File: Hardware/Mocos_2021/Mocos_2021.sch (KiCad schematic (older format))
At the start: 104 parts, among them IC1 TC2117, J1 USB_B_Mini, J2 SERIAL PORT, J3 Programming, Q1 IRFS7530, Q2 IRFS7530, Q3 IRFS7530, Q4 IRFS7530, Q5 IRFS7530, Q6 IRFS7530, U1 DRV8302, U2 STM32F40X_LQFP64, X1 8MHz, 10ppm

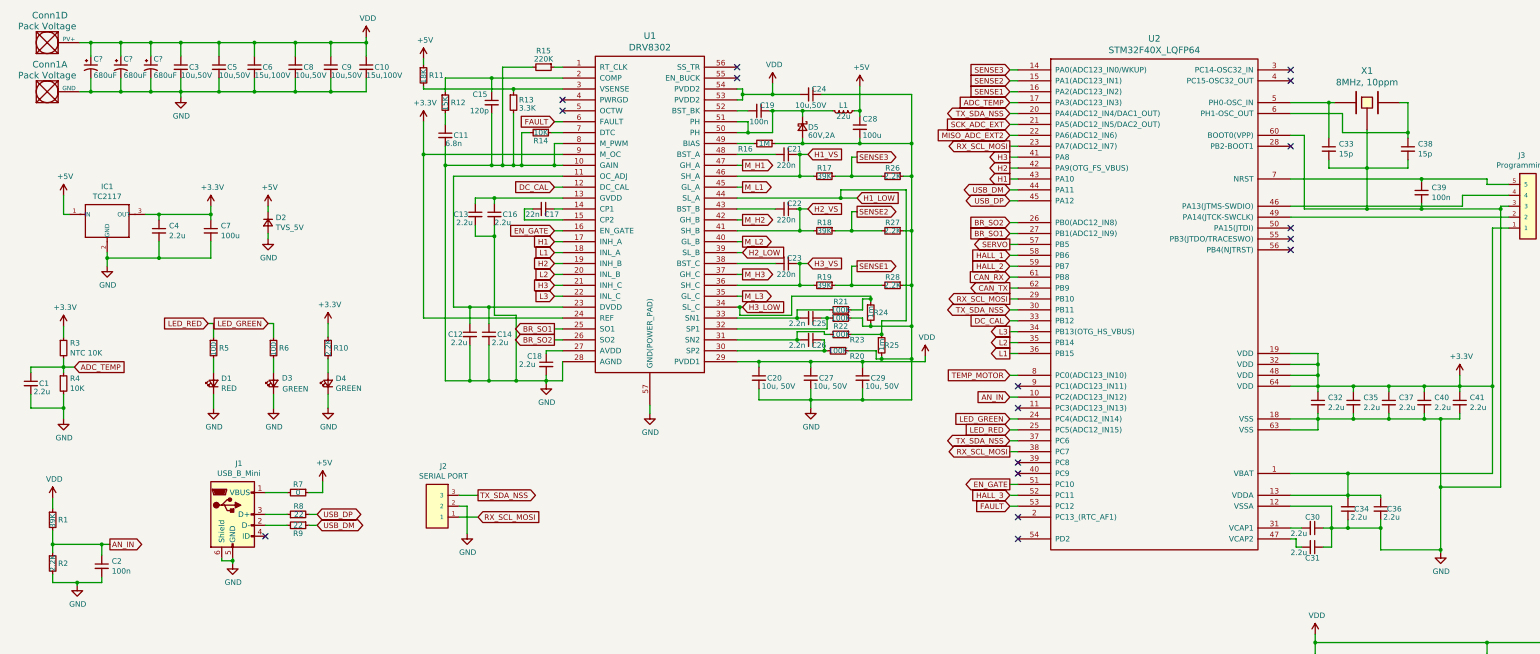
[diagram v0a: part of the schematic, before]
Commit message: Added footprints to board
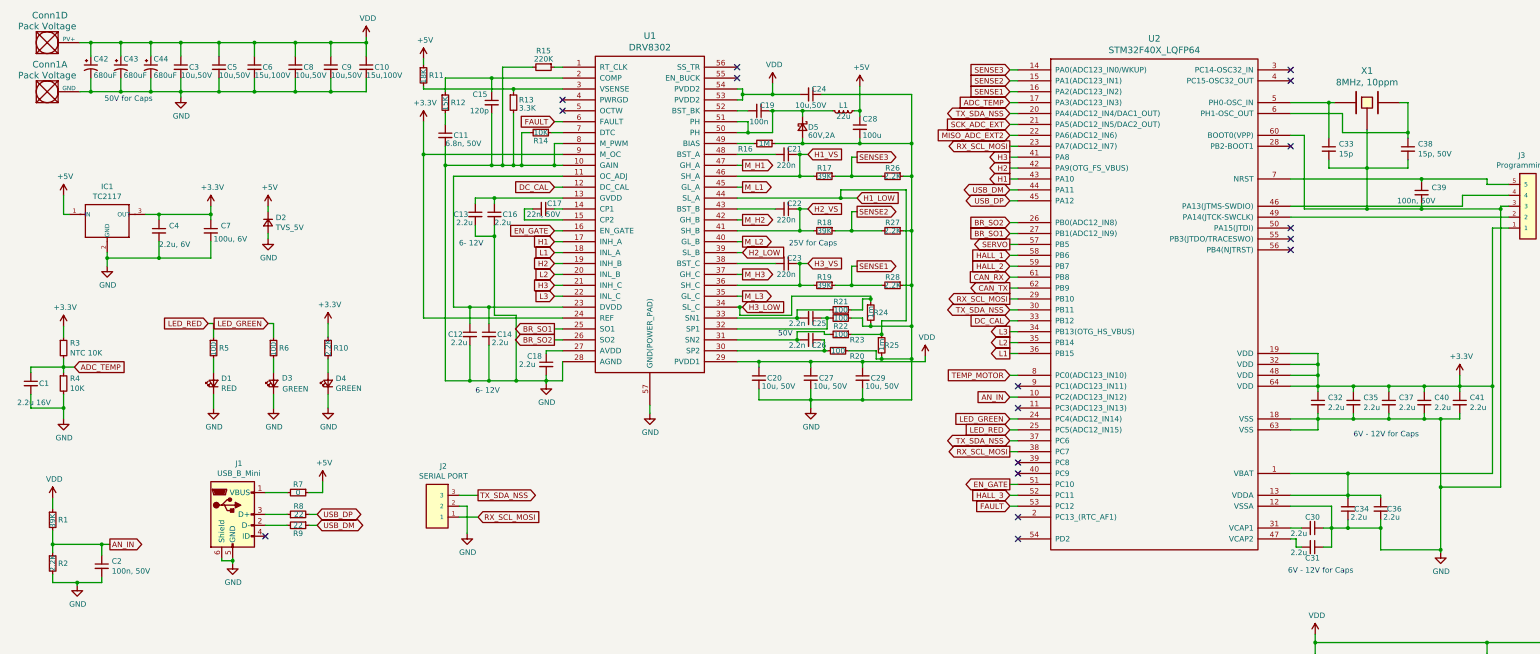
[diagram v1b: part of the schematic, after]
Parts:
- C1: value 2.2u -> 2.2u 16V; footprint Capacitor_SMD:C_1206_3216Metric_Pad1.33x1.80mm_HandSolder -> Capacitor_SMD:C_0402_1005Metric_Pad0.74x0.62mm_HandSolder
- C10, C28, C6: footprint (none) -> Capacitor_SMD:C_2220_5650Metric_Pad1.97x5.40mm_HandSolder
- C11: value 6.8n -> 6.8n, 50V; footprint (none) -> Capacitor_SMD:C_0603_1608Metric_Pad1.08x0.95mm_HandSolder
- C12, C13, C14, C15, C16, C18, C25, C26, C30, C31, C32, C34, C35, C36, C37, C40, C41: footprint (none) -> Capacitor_SMD:C_0402_1005Metric_Pad0.74x0.62mm_HandSolder
- C17: value 22n -> 22n, 50V; footprint (none) -> Capacitor_SMD:C_0402_1005Metric_Pad0.74x0.62mm_HandSolder
- C19, C33: footprint (none) -> Capacitor_SMD:C_0603_1608Metric_Pad1.08x0.95mm_HandSolder
- C2: value 100n -> 100n, 50V
- C20, C24, C27, C29, C5, C8, C9: footprint (none) -> Capacitor_SMD:C_1210_3225Metric_Pad1.33x2.70mm_HandSolder
- C21, C22, C23: footprint (none) -> Capacitor_SMD:C_0805_2012Metric_Pad1.18x1.45mm_HandSolder
- C3: footprint Capacitor_SMD:C_0603_1608Metric_Pad1.08x0.95mm_HandSolder -> Capacitor_SMD:C_1210_3225Metric_Pad1.33x2.70mm_HandSolder
- C38: value 15p -> 15p, 50V; footprint (none) -> Capacitor_SMD:C_0603_1608Metric_Pad1.08x0.95mm_HandSolder
- C39: value 100n -> 100n, 50V; footprint (none) -> Capacitor_SMD:C_0603_1608Metric_Pad1.08x0.95mm_HandSolder
- C4: value 2.2u -> 2.2u, 6V; footprint (none) -> Capacitor_SMD:C_0402_1005Metric_Pad0.74x0.62mm_HandSolder
- C42, C43, C44: renamed from C?; footprint (none) -> Capacitor_THT:CP_Radial_D16.0mm_P7.50mm
- C7: value 100u -> 100u, 6V; footprint (none) -> Capacitor_SMD:C_0402_1005Metric_Pad0.74x0.62mm_HandSolder
- Conn1: footprint (none) -> MRDT_Connectors:Anderson_2_Vertical_Sidy_by_Side
- Conn2, Conn3, Conn4: footprint (none) -> MRDT_Connectors:Anderson_2_Horizontal_Side_by_Side
- D1, D3, D4: footprint (none) -> LED_SMD:LED_0603_1608Metric_Pad1.05x0.95mm_HandSolder
- D2: footprint (none) -> Diode_SMD:D_SMA_Handsoldering
- D5: footprint (none) -> Diode_SMD:D_SOD-123F
- J1: footprint (none) -> crf1:mini_USB_gnd
- L1: footprint (none) -> crf1:inductor_74435580680
- Q1, Q2, Q3, Q4, Q5, Q6: footprint (none) -> Package_TO_SOT_SMD:TO-263-7_TabPin4
- R1, R10, R11, R12, R13, R14, R15, R16, R17, R18, R19, R2, R26, R27, R28, R29, R3, R30, R31, R32, R33, R34, R35, R36, R37, R4, R5, R6, R7, R8, R9: footprint (none) -> Resistor_SMD:R_0603_1608Metric_Pad0.98x0.95mm_HandSolder
- R20, R21, R22, R23: value 100K -> 100; footprint (none) -> Resistor_SMD:R_0603_1608Metric_Pad0.98x0.95mm_HandSolder
- R24, R25: footprint (none) -> crf1:WSLP2726
- U1: footprint (none) -> crf1:TSSOP-56-PP
- U2: footprint (none) -> crf1:lqfp64_pad_mod
- X1: footprint (none) -> crf1:Crystal_5x3mm
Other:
- note added: "25V for Caps"
- note added: "50V"
- note added: "50V for Caps"
- note added: "6- 12V"
- note added: "6V - 12V for Caps"

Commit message: Finished STM32 Layout
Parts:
- removed unit 1 of Conn2
- removed unit 1 of Conn3
- removed unit 1 of Conn4
- removed R7: 0, Resistor_SMD:R_0603_1608Metric_Pad0.98x0.95mm_HandSolder, symbol Device:R_Small
- removed X1: 8MHz, 10ppm, crf1:Crystal_5x3mm, symbol crf_1:CRYSTAL_GROUND_PIN
- added X1: 8MHz, 10ppm, crf1:Crystal_5x3mm, symbol crf_1:CRYSTAL_SMD
- Conn1: footprint MRDT_Connectors:Anderson_2_Vertical_Sidy_by_Side -> MRDT_Connectors:Anderson_2_Horizontal_Side_by_Side_PV
- Conn2: value Phase1 -> Phases; footprint MRDT_Connectors:Anderson_2_Horizontal_Side_by_Side -> MRDT_Connectors:Anderson_3_Horizontal_Side_by_Side
- Conn2: renamed from Conn3; value Phase2 -> Phases; footprint MRDT_Connectors:Anderson_2_Horizontal_Side_by_Side -> MRDT_Connectors:Anderson_3_Horizontal_Side_by_Side
- Conn2: renamed from Conn4; value Phase3 -> Phases; footprint MRDT_Connectors:Anderson_2_Horizontal_Side_by_Side -> MRDT_Connectors:Anderson_3_Horizontal_Side_by_Side
- IC1: footprint crf1:v-reg-78XXS -> crf1:SOT-223
- J1: footprint crf1:mini_USB_gnd -> crf1:USB-UX60R-MB-5ST
- J2: footprint MRDT_Connectors:MOLEX_uF_S_03_Vertical -> MRDT_Connectors:MOLEX_uF_S_03_Horizontal
- J3: footprint MRDT_Connectors:MOLEX_uF_S_05_Vertical -> MRDT_Connectors:MOLEX_uF_S_05_Horizontal
- Q1, Q2, Q3, Q4, Q5, Q6: value IRFS7530 -> IRFZ44ESTRLPBF; footprint Package_TO_SOT_SMD:TO-263-7_TabPin4 -> Package_TO_SOT_SMD:TO-263-3_TabPin4
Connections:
- net GND: now also X1.2 (GND/NC), X1.4 (GND/NC)
- net H1_VS: now also Conn2.1 (GND); no longer Conn2.4 (PV+)
- net H2_VS: now also Conn2.2 (V+Log); no longer Conn2.4 (PV+)
- net H3_VS: now also Conn2.3 (V+Act); no longer Conn2.4 (PV+)
- net at C33.1, U2.5 (PH0-OSC_IN): now also X1.1 (CLK)
- net at C38.1, U2.6 (PH1-OSC_OUT): now also X1.3 (CLK)
- net USB_DM renamed USB-
- net USB_DP renamed USB+
- no-connect marks 17 -> 18

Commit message: Added 3.3V Oki for cleaner layout
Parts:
- removed C11: 6.8n, 50V, Capacitor_SMD:C_0603_1608Metric_Pad1.08x0.95mm_HandSolder, symbol Device:C_Small
- removed C15: 120p, Capacitor_SMD:C_0402_1005Metric_Pad0.74x0.62mm_HandSolder, symbol Device:C_Small
- removed C19: 100n, Capacitor_SMD:C_0603_1608Metric_Pad1.08x0.95mm_HandSolder, symbol Device:C_Small
- removed C24: 10u,50V, Capacitor_SMD:C_1210_3225Metric_Pad1.33x2.70mm_HandSolder, symbol Device:C_Small
- removed C28: 100u, Capacitor_SMD:C_2220_5650Metric_Pad1.97x5.40mm_HandSolder, symbol Device:C_Small
- removed D2: TVS_5V, Diode_SMD:D_SMA_Handsoldering, symbol Device:D_Small
- removed D5: 60V,2A, Diode_SMD:D_SOD-123F, symbol Device:D_Schottky_Small
- removed IC1: TC2117, crf1:SOT-223, symbol crf_1:V-reg
- removed L1: 22u, crf1:inductor_74435580680, symbol Device:L_Small
- removed R11: 18K, Resistor_SMD:R_0603_1608Metric_Pad0.98x0.95mm_HandSolder, symbol Device:R_Small
- removed R12: 15K, Resistor_SMD:R_0603_1608Metric_Pad0.98x0.95mm_HandSolder, symbol Device:R_Small
- removed R13: 3.3K, Resistor_SMD:R_0603_1608Metric_Pad0.98x0.95mm_HandSolder, symbol Device:R_Small
- removed R24, R25: 1m, crf1:WSLP2726, symbol Device:R_Small
- added R11, R7: 1m, crf1:WSLP2726, symbol crf_1:SHUNT
- added U3: 3.3V OKI, MRDT_Devices:OKI_Horizontal, symbol MRDT_Devices:OKI
- Q1, Q2, Q3, Q4, Q5, Q6: footprint Package_TO_SOT_SMD:TO-263-3_TabPin4 -> MRDT_Actives:IRFZ44ESTRLPBF
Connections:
- net +3V3: now also U3.3 (Vo)
- net GND: now also R11.2, R7.2, U3.2 (GND); no longer R20.1, R22.1
- net H1_LOW: now also R7.1; no longer R23.1
- net H3_LOW: now also R11.1; no longer R21.1
- net VDD: now also U3.1 (Vi); no longer U1.53 (PVDD2), U1.54 (PVDD2)
- net at U1.50 (PH): no longer U1.51 (PH)
- net CAN_RX: no longer names the net of U2.61 (PB8)
- net CAN_TX: no longer names the net of U2.62 (PB9)
- net HALL_1: no longer names the net of U2.58 (PB6)
- net HALL_2: no longer names the net of U2.59 (PB7)
- net HALL_3: no longer names the net of U2.52 (PC11)
- net SERVO: no longer names the net of U2.57 (PB5)
- net TEMP_MOTOR: no longer names the net of U2.8 (PC0(ADC123_IN10))
- new net: R20.1, R7.4
- new net: R23.1, R7.3
- new net: R11.4, R22.1
- new net: R11.3, R21.1
- no-connect marks 18 -> 32
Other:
- note added: "Connectors"
- note added: "Indicators"
- note added: "MCU"
- note added: "Mosfet Driver"
- note added: "Mosfets"
- note added: "Power"
- note added: "Temperature Sense and Analog In"
- moved on the sheet: C1, C10, C12, C13, C14, C16, C17, C18, C2, C20, C21, C22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

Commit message: Finished layout and generated Gerbs
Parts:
- U1: value DRV8302 -> DRV8302DCA
- U2: value STM32F40X_LQFP64 -> STM32F405RGT6
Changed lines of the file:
@@
 P 12825 3625
 F 0 "U2" H 12825 6062 60  0000 C CNN
-F 1 "STM32F40X_LQFP64" H 12825 5956 60  0000 C CNN
+F 1 "STM32F405RGT6" H 12825 5956 60  0000 C CNN
 F 2 "crf1:lqfp64_pad_mod" H 12825 3625 60  0001 C CNN
 F 3 "" H 12825 3625 60  0000 C CNN
@@
 AR Path="/613C4F07" Ref="U1"  Part="1"
 F 0 "U1" H 6800 4262 60  0000 C CNN
-F 1 "DRV8302" H 6800 4156 60  0000 C CNN
+F 1 "DRV8302DCA" H 6800 4156 60  0000 C CNN
 F 2 "crf1:TSSOP-56-PP" H 6800 2625 60  0001 C CNN
 F 3 "" H 6800 2625 60  0000 C CNN

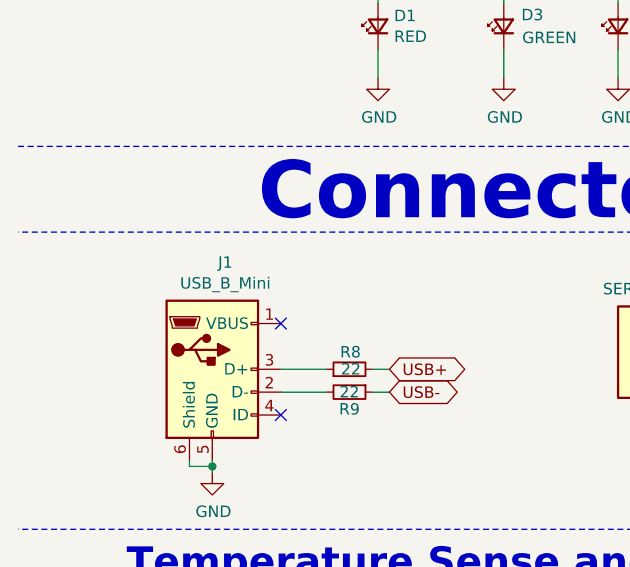
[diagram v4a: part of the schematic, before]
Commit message: Finished BOM and Fixed some Layout errors such as trace tolerance
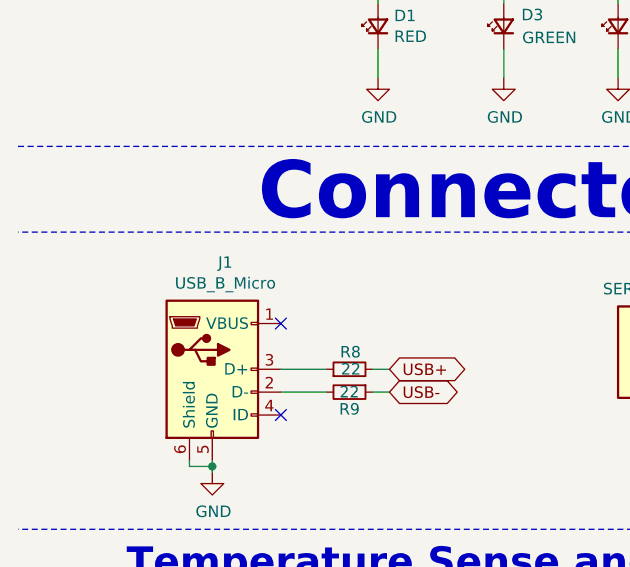
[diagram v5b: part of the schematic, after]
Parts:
- removed J1: USB_B_Mini, crf1:USB-UX60R-MB-5ST, symbol Connector:USB_B_Mini
- added J1: USB_B_Micro, MRDT_Connectors:MOLEX_47346-0001, symbol Connector:USB_B_Micro
- C7: footprint Capacitor_SMD:C_0402_1005Metric_Pad0.74x0.62mm_HandSolder -> Capacitor_SMD:C_0805_2012Metric_Pad1.18x1.45mm_HandSolder
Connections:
- net GND: now also J1.5 (GND), J1.6 (Shield)
- net at R9.2: now also J1.2 (D-)
- net at R8.1: now also J1.3 (D+)
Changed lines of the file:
@@
 F 0 "C7" H 3367 2671 50  0000 L CNN
 F 1 "100u, 6V" H 3300 2550 50  0000 L CNN
-F 2 "Capacitor_SMD:C_0402_1005Metric_Pad0.74x0.62mm_HandSolder" H 3275 2625 50  0001 C CNN
+F 2 "Capacitor_SMD:C_0805_2012Metric_Pad1.18x1.45mm_HandSolder" H 3275 2625 50  0001 C CNN
 F 3 "~" H 3275 2625 50  0001 C CNN
 	1    3275 2625
@@
 	3500 7650 3575 7650
 Connection ~ 3500 7650
-$Comp
-L Connector:USB_B_Mini J1
-U 1 1 6231FC2B
-P 1325 5975
-F 0 "J1" H 1382 6442 50  0000 C CNN
-F 1 "USB_B_Mini" H 1382 6351 50  0000 C CNN
-F 2 "crf1:USB-UX60R-MB-5ST" H 1475 5925 50  0001 C CNN
-F 3 "~" H 1475 5925 50  0001 C CNN
-	1    1325 5975
-	1    0    0    -1
-$EndComp
 $Comp
 L power:GND #PWR010
@@
 	9200 4475 9200 4325
 Connection ~ 9200 4325
+$Comp
+L Connector:USB_B_Micro J1
+U 1 1 612C88A1
+P 1325 5975
+F 0 "J1" H 1382 6442 50  0000 C CNN
+F 1 "USB_B_Micro" H 1382 6351 50  0000 C CNN
+F 2 "MRDT_Connectors:MOLEX_47346-0001" H 1475 5925 50  0001 C CNN
+F 3 "~" H 1475 5925 50  0001 C CNN
+	1    1325 5975
+	1    0    0    -1
+$EndComp
 $EndSCHEMATC
